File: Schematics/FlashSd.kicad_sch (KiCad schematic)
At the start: 4 parts, among them J8 Micro_SD_Card

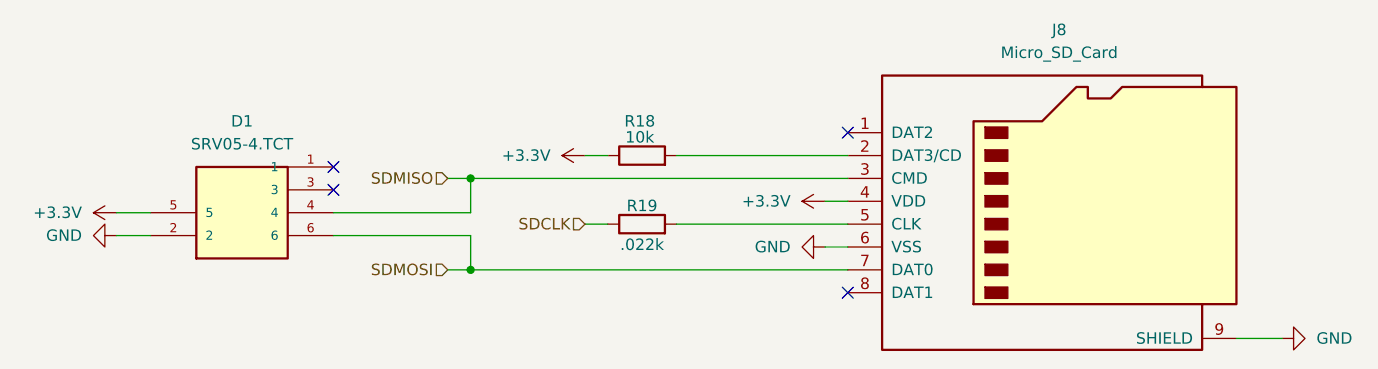
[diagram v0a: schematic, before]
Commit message: added LCSC numbers and footprint values, need to connect schemeatic pins, then can start layout
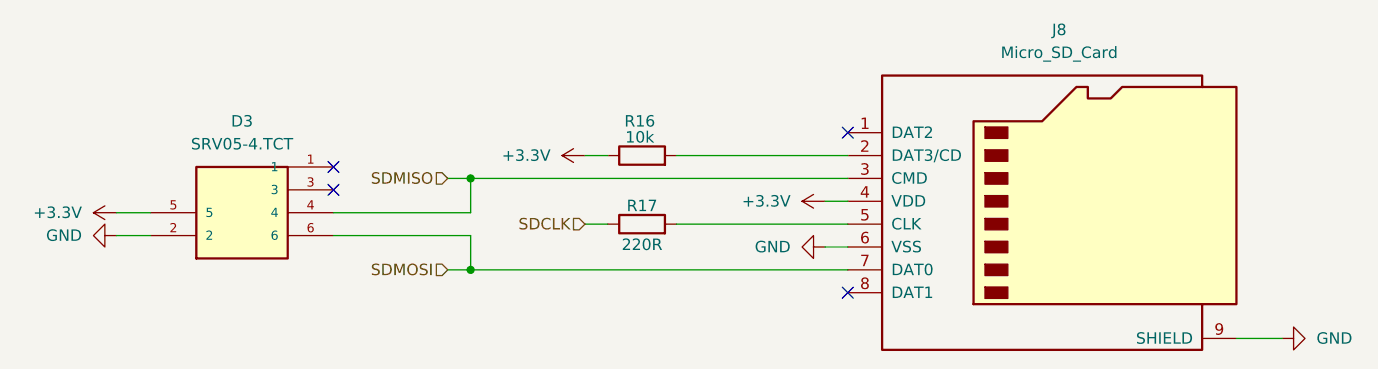
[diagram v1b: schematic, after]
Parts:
- D3: renamed from D1; LCSC Part (none) -> C13612
- J8: footprint (none) -> Connector_Card:microSD_HC_Molex_104031-0811; LCSC Part (none) -> C164170
- R16: renamed from R18; footprint (none) -> Resistor_SMD:R_0805_2012Metric_Pad1.20x1.40mm_HandSolder; LCSC Part (none) -> C84376
- R17: renamed from R19; value .022k -> 220R; footprint (none) -> Resistor_SMD:R_0805_2012Metric_Pad1.20x1.40mm_HandSolder; LCSC Part (none) -> C17557
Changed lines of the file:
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@@
 		(on_board yes)
 		(dnp no)
-		(property "Reference" "#PWR043"
+		(property "Reference" "#PWR061"
 			(at 172.72 96.52 0)
 			(effects
@@
 			(project ""
 				(path "/6cb3dda3-5fe8-4715-b831-354360aa3199/caa4144d-1f54-4913-83e9-888ee3d0dcec"
-					(reference "#PWR043")
+					(reference "#PWR061")
 					(unit 1)
 				)
@@
 		(dnp no)
 		(fields_autoplaced yes)
-		(property "Reference" "#PWR08"
+		(property "Reference" "#PWR063"
 			(at 226.06 111.76 0)
 			(effects
@@
 			(project ""
 				(path "/6cb3dda3-5fe8-4715-b831-354360aa3199/caa4144d-1f54-4913-83e9-888ee3d0dcec"
-					(reference "#PWR08")
+					(reference "#PWR063")
 					(unit 1)
 				)
@@
 		(on_board yes)
 		(dnp no)
-		(property "Reference" "D1"
+		(property "Reference" "D3"
 			(at 104.14 87.63 0)
 			(effects
@@
 				)
 				(justify bottom)
+				(hide yes)
+			)
+		)
+		(property "Sim.Device" ""
+			(at 93.98 95.25 0)
+			(effects
+				(font
+					(size 1.27 1.27)
+				)
+				(hide yes)
+			)
+		)
+		(property "Sim.Type" ""
+			(at 93.98 95.25 0)
+			(effects
+				(font
+					(size 1.27 1.27)
+				)
+				(hide yes)
+			)
+		)
+		(property "LCSC Part" "C13612"
+			(at 93.98 95.25 0)
+			(effects
+				(font
+					(size 1.27 1.27)
+				)
 				(hide yes)
 			)
@@
 			(project "flightcomputer2"
 				(path "/6cb3dda3-5fe8-4715-b831-354360aa3199/caa4144d-1f54-4913-83e9-888ee3d0dcec"
-					(reference "D1")
+					(reference "D3")
 					(unit 1)
 				)
@@
 		(dnp no)
 		(fields_autoplaced yes)
-		(property "Reference" "#PWR045"
+		(property "Reference" "#PWR059"
 			(at 83.82 100.33 0)
 			(effects
@@
 			(project ""
 				(path "/6cb3dda3-5fe8-4715-b831-354360aa3199/caa4144d-1f54-4913-83e9-888ee3d0dcec"
-					(reference "#PWR045")
+					(reference "#PWR059")
 					(unit 1)
 				)
@@
 		(on_board yes)
 		(dnp no)
-		(property "Reference" "R18"
+		(property "Reference" "R16"
 			(at 148.336 87.63 90)
 			(effects
@@
 			)
 		)
-		(property "Footprint" ""
+		(property "Footprint" "Resistor_SMD:R_0805_2012Metric_Pad1.20x1.40mm_HandSolder"
 			(at 148.59 93.218 90)
 			(effects
@@
 		(property "Description" "Resistor"
 			(at 148.59 91.44 0)
+			(effects
+				(font
+					(size 1.27 1.27)
+				)
+				(hide yes)
+			)
+		)
+		(property "Sim.Device" ""
+			(at 148.59 91.44 90)
+			(effects
+				(font
+					(size 1.27 1.27)
+				)
+				(hide yes)
+			)
+		)
+		(property "Sim.Type" ""
+			(at 148.59 91.44 90)
+			(effects
+				(font
+					(size 1.27 1.27)
+				)
+				(hide yes)
+			)
+		)
+		(property "LCSC Part" "C84376"
+			(at 148.59 91.44 90)
 			(effects
 				(font
@@
 			(project ""
 				(path "/6cb3dda3-5fe8-4715-b831-354360aa3199/caa4144d-1f54-4913-83e9-888ee3d0dcec"
-					(reference "R18")
+					(reference "R16")
 					(unit 1)
 				)
@@
 		(on_board yes)
 		(dnp no)
-		(property "Reference" "R19"
+		(property "Reference" "R17"
 			(at 148.59 97.028 90)
 			(effects
@@
 			)
 		)
-		(property "Value" ".022k"
+		(property "Value" "220R"
 			(at 148.59 101.346 90)
 			(effects
@@
 			)
 		)
-		(property "Footprint" ""
+		(property "Footprint" "Resistor_SMD:R_0805_2012Metric_Pad1.20x1.40mm_HandSolder"
 			(at 148.59 100.838 90)
 			(effects
@@
 		(property "Description" "Resistor"
 			(at 148.59 99.06 0)
+			(effects
+				(font
+					(size 1.27 1.27)
+				)
+				(hide yes)
+			)
+		)
+		(property "Sim.Device" ""
+			(at 148.59 99.06 90)
+			(effects
+				(font
+					(size 1.27 1.27)
+				)
+				(hide yes)
+			)
+		)
+		(property "Sim.Type" ""
+			(at 148.59 99.06 90)
+			(effects
+				(font
+					(size 1.27 1.27)
+				)
+				(hide yes)
+			)
+		)
+		(property "LCSC Part" "C17557"
+			(at 148.59 99.06 90)
 			(effects
 				(font
@@
 			(project ""
 				(path "/6cb3dda3-5fe8-4715-b831-354360aa3199/caa4144d-1f54-4913-83e9-888ee3d0dcec"
-					(reference "R19")
+					(reference "R17")
 					(unit 1)
 				)
@@
 		(dnp no)
 		(fields_autoplaced yes)
-		(property "Reference" "#PWR044"
+		(property "Reference" "#PWR058"
 			(at 93.98 97.79 0)
 			(effects
@@
 			(project ""
 				(path "/6cb3dda3-5fe8-4715-b831-354360aa3199/caa4144d-1f54-4913-83e9-888ee3d0dcec"
-					(reference "#PWR044")
+					(reference "#PWR058")
 					(unit 1)
 				)
@@
 		(dnp no)
 		(fields_autoplaced yes)
-		(property "Reference" "#PWR046"
+		(property "Reference" "#PWR062"
 			(at 162.56 101.6 0)
 			(effects
@@
 			(project ""
 				(path "/6cb3dda3-5fe8-4715-b831-354360aa3199/caa4144d-1f54-4913-83e9-888ee3d0dcec"
-					(reference "#PWR046")
+					(reference "#PWR062")
 					(unit 1)
 				)
@@
 			)
 		)
-		(property "Footprint" ""
+		(property "Footprint" "Connector_Card:microSD_HC_Molex_104031-0811"
 			(at 223.52 88.9 0)
 			(effects
@@
 		)
 		(property "Description" "Micro SD Card Socket"
+			(at 194.31 96.52 0)
+			(effects
+				(font
+					(size 1.27 1.27)
+				)
+				(hide yes)
+			)
+		)
+		(property "LCSC Part" "C164170"
+			(at 194.31 96.52 0)
+			(effects
+				(font
+					(size 1.27 1.27)
+				)
+				(hide yes)
+			)
+		)
+		(property "Sim.Device" ""
+			(at 194.31 96.52 0)
+			(effects
+				(font
+					(size 1.27 1.27)
+				)
+				(hide yes)
+			)
+		)
+		(property "Sim.Type" ""
 			(at 194.31 96.52 0)
 			(effects
@@
 		(dnp no)
 		(fields_autoplaced yes)
-		(property "Reference" "#PWR070"
+		(property "Reference" "#PWR060"
 			(at 146.05 91.44 0)
 			(effects
@@
 			(project ""
 				(path "/6cb3dda3-5fe8-4715-b831-354360aa3199/caa4144d-1f54-4913-83e9-888ee3d0dcec"
-					(reference "#PWR070")
+					(reference "#PWR060")
 					(unit 1)
 				)

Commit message: started lora schematic all pcb parts should be included
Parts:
- D3: DESCRIPTION Semtech SRV05-4.TCT, Uni-Directional TVS Diode Array, 300W,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 -> (none); Description_1 ESD Suppressors / TVS Diodes SOT-23 5V 4DIODE Low Capacitan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 -> (none); MF UMW -> (none); MOUSER_PART_NUMBER 947-SRV05-4.TCT -> (none); MOUSER_PRICE-STOCK https://www.mouser.com/Search/Refine.aspx?Keyword=947-SRV05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 -> (none); MP SRV05-4.TCT -> (none); Package None -> (none); Price None -> (none)
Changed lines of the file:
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@@
 			)
 		)
-		(property "MF" "UMW"
+		(property "Check_prices" "https://www.snapeda.com/parts/SRV05-4.TCT/UMW/view-part/?ref=eda"
 			(at 93.98 95.25 0)
 			(effects
@@
 			)
 		)
-		(property "MOUSER_PRICE-STOCK" "https://www.mouser.com/Search/Refine.aspx?Keyword=947-SRV05-4.TCT"
+		(property "HEIGHT" "1.45mm"
 			(at 93.98 95.25 0)
 			(effects
@@
 			)
 		)
-		(property "DESCRIPTION" "Semtech SRV05-4.TCT, Uni-Directional TVS Diode Array, 300W, 6-Pin SOT-23"
+		(property "SnapEDA_Link" "https://www.snapeda.com/parts/SRV05-4.TCT/UMW/view-part/?ref=snap"
 			(at 93.98 95.25 0)
 			(effects
@@
 			)
 		)
-		(property "MOUSER_PART_NUMBER" "947-SRV05-4.TCT"
+		(property "Availability" "In Stock"
 			(at 93.98 95.25 0)
 			(effects
@@
 			)
 		)
-		(property "Price" "None"
+		(property "MANUFACTURER_PART_NUMBER" "SRV05-4.TCT"
 			(at 93.98 95.25 0)
 			(effects
@@
 				)
 				(justify bottom)
-				(hide yes)
-			)
-		)
-		(property "Package" "None"
-			(at 93.98 95.25 0)
-			(effects
-				(font
-					(size 1.27 1.27)
-				)
-				(justify bottom)
-				(hide yes)
-			)
-		)
-		(property "Check_prices" "https://www.snapeda.com/parts/SRV05-4.TCT/UMW/view-part/?ref=eda"
-			(at 93.98 95.25 0)
-			(effects
-				(font
-					(size 1.27 1.27)
-				)
-				(justify bottom)
-				(hide yes)
-			)
-		)
-		(property "HEIGHT" "1.45mm"
-			(at 93.98 95.25 0)
-			(effects
-				(font
-					(size 1.27 1.27)
-				)
-				(justify bottom)
-				(hide yes)
-			)
-		)
-		(property "SnapEDA_Link" "https://www.snapeda.com/parts/SRV05-4.TCT/UMW/view-part/?ref=snap"
-			(at 93.98 95.25 0)
-			(effects
-				(font
-					(size 1.27 1.27)
-				)
-				(justify bottom)
-				(hide yes)
-			)
-		)
-		(property "MP" "SRV05-4.TCT"
-			(at 93.98 95.25 0)
-			(effects
-				(font
-					(size 1.27 1.27)
-				)
-				(justify bottom)
-				(hide yes)
-			)
-		)
-		(property "Description_1" "ESD Suppressors / TVS Diodes SOT-23 5V 4DIODE Low Capacitance"
-			(at 93.98 95.25 0)
-			(effects
-				(font
-					(size 1.27 1.27)
-				)
-				(justify bottom)
-				(hide yes)
-			)
-		)
-		(property "Availability" "In Stock"
-			(at 93.98 95.25 0)
-			(effects
-				(font
-					(size 1.27 1.27)
-				)
-				(justify bottom)
-				(hide yes)
-			)
-		)
-		(property "MANUFACTURER_PART_NUMBER" "SRV05-4.TCT"
-			(at 93.98 95.25 0)
-			(effects
-				(font
-					(size 1.27 1.27)
-				)
-				(justify bottom)
-				(hide yes)
-			)
-		)
-		(property "Sim.Device" ""
-			(at 93.98 95.25 0)
-			(effects
-				(font
-					(size 1.27 1.27)
-				)
-				(hide yes)
-			)
-		)
-		(property "Sim.Type" ""
-			(at 93.98 95.25 0)
-			(effects
-				(font
-					(size 1.27 1.27)
-				)
 				(hide yes)
 			)
@@
 			)
 		)
-		(property "Sim.Device" ""
-			(at 148.59 91.44 90)
-			(effects
-				(font
-					(size 1.27 1.27)
-				)
-				(hide yes)
-			)
-		)
-		(property "Sim.Type" ""
-			(at 148.59 91.44 90)
-			(effects
-				(font
-					(size 1.27 1.27)
-				)
-				(hide yes)
-			)
-		)
 		(property "LCSC Part" "C84376"
 			(at 148.59 91.44 90)
@@
 		(property "Description" "Resistor"
 			(at 148.59 99.06 0)
-			(effects
-				(font
-					(size 1.27 1.27)
-				)
-				(hide yes)
-			)
-		)
-		(property "Sim.Device" ""
-			(at 148.59 99.06 90)
-			(effects
-				(font
-					(size 1.27 1.27)
-				)
-				(hide yes)
-			)
-		)
-		(property "Sim.Type" ""
-			(at 148.59 99.06 90)
 			(effects
 				(font
@@
 			(at 194.31 96.52 0)
 			(effects
-				(font
-					(size 1.27 1.27)
-				)
-				(hide yes)
-			)
-		)
-		(property "Sim.Device" ""
-			(at 194.31 96.52 0)
-			(effects
-				(font
-					(size 1.27 1.27)
-				)
-				(hide yes)
-			)
-		)
-		(property "Sim.Type" ""
-			(at 194.31 96.52 0)
-			(effects

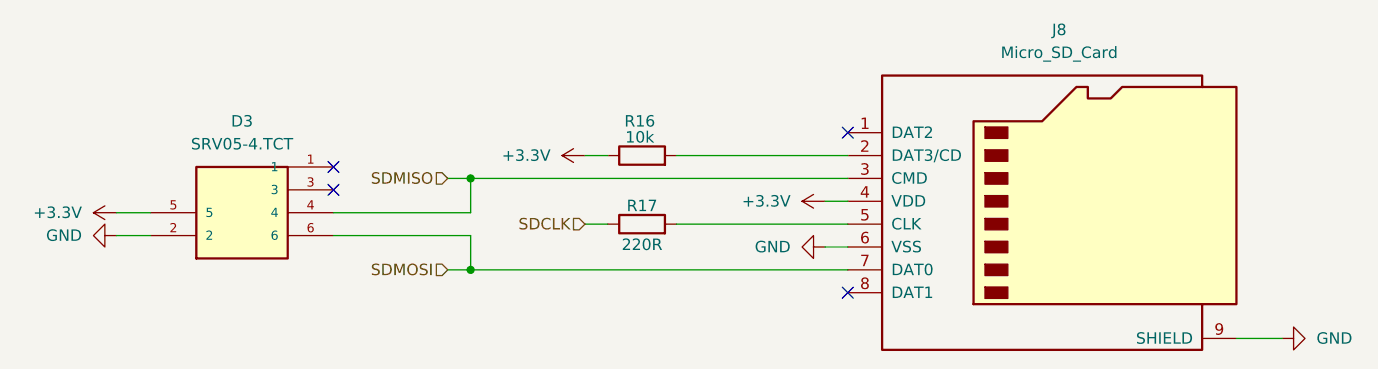
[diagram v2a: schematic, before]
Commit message: added lora correct and organizing sheet pins
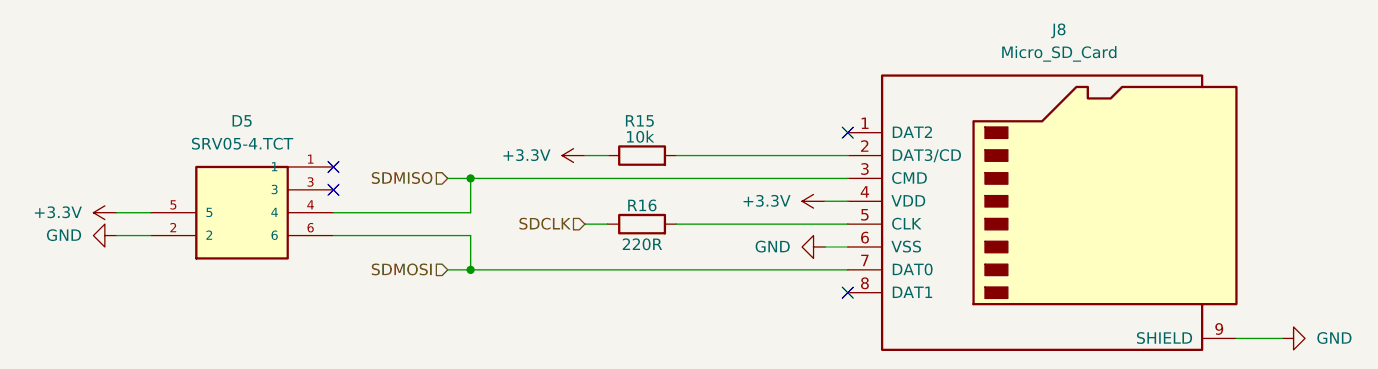
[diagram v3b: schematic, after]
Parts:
- J8: footprint Connector_Card:microSD_HC_Molex_104031-0811 -> Connector_Card:microSD_HC_Molex_47219-2001
- renumbered D3 to D5, R16 to R15, R17 to R16
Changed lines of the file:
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@@
 		(on_board yes)
 		(dnp no)
-		(property "Reference" "#PWR061"
+		(property "Reference" "#PWR064"
 			(at 172.72 96.52 0)
 			(effects
@@
 			(project ""
 				(path "/6cb3dda3-5fe8-4715-b831-354360aa3199/caa4144d-1f54-4913-83e9-888ee3d0dcec"
-					(reference "#PWR061")
+					(reference "#PWR064")
 					(unit 1)
 				)
@@
 		(dnp no)
 		(fields_autoplaced yes)
-		(property "Reference" "#PWR063"
+		(property "Reference" "#PWR066"
 			(at 226.06 111.76 0)
 			(effects
@@
 			(project ""
 				(path "/6cb3dda3-5fe8-4715-b831-354360aa3199/caa4144d-1f54-4913-83e9-888ee3d0dcec"
-					(reference "#PWR063")
+					(reference "#PWR066")
 					(unit 1)
 				)
@@
 		(on_board yes)
 		(dnp no)
-		(property "Reference" "D3"
+		(property "Reference" "D5"
 			(at 104.14 87.63 0)
 			(effects
@@
 			(project "flightcomputer2"
 				(path "/6cb3dda3-5fe8-4715-b831-354360aa3199/caa4144d-1f54-4913-83e9-888ee3d0dcec"
-					(reference "D3")
+					(reference "D5")
 					(unit 1)
 				)
@@
 		(dnp no)
 		(fields_autoplaced yes)
-		(property "Reference" "#PWR059"
+		(property "Reference" "#PWR062"
 			(at 83.82 100.33 0)
 			(effects
@@
 			(project ""
 				(path "/6cb3dda3-5fe8-4715-b831-354360aa3199/caa4144d-1f54-4913-83e9-888ee3d0dcec"
-					(reference "#PWR059")
+					(reference "#PWR062")
 					(unit 1)
 				)
@@
 		(on_board yes)
 		(dnp no)
-		(property "Reference" "R16"
+		(property "Reference" "R15"
 			(at 148.336 87.63 90)
 			(effects
@@
 			(project ""
 				(path "/6cb3dda3-5fe8-4715-b831-354360aa3199/caa4144d-1f54-4913-83e9-888ee3d0dcec"
-					(reference "R16")
+					(reference "R15")
 					(unit 1)
 				)
@@
 		(on_board yes)
 		(dnp no)
-		(property "Reference" "R17"
+		(property "Reference" "R16"
 			(at 148.59 97.028 90)
 			(effects
@@
 			(project ""
 				(path "/6cb3dda3-5fe8-4715-b831-354360aa3199/caa4144d-1f54-4913-83e9-888ee3d0dcec"
-					(reference "R17")
+					(reference "R16")
 					(unit 1)
 				)
@@
 		(dnp no)
 		(fields_autoplaced yes)
-		(property "Reference" "#PWR058"
+		(property "Reference" "#PWR061"
 			(at 93.98 97.79 0)
 			(effects
@@
 			(project ""
 				(path "/6cb3dda3-5fe8-4715-b831-354360aa3199/caa4144d-1f54-4913-83e9-888ee3d0dcec"
-					(reference "#PWR058")
+					(reference "#PWR061")
 					(unit 1)
 				)
@@
 		(dnp no)
 		(fields_autoplaced yes)
-		(property "Reference" "#PWR062"
+		(property "Reference" "#PWR065"
 			(at 162.56 101.6 0)
 			(effects
@@
 			(project ""
 				(path "/6cb3dda3-5fe8-4715-b831-354360aa3199/caa4144d-1f54-4913-83e9-888ee3d0dcec"
-					(reference "#PWR062")
+					(reference "#PWR065")
 					(unit 1)
 				)
@@
 			)
 		)
-		(property "Footprint" "Connector_Card:microSD_HC_Molex_104031-0811"
+		(property "Footprint" "Connector_Card:microSD_HC_Molex_47219-2001"
 			(at 223.52 88.9 0)
 			(effects
@@
 		(dnp no)
 		(fields_autoplaced yes)
-		(property "Reference" "#PWR060"
+		(property "Reference" "#PWR063"
 			(at 146.05 91.44 0)
 			(effects
@@
 			(project ""
 				(path "/6cb3dda3-5fe8-4715-b831-354360aa3199/caa4144d-1f54-4913-83e9-888ee3d0dcec"
-					(reference "#PWR060")
-					(unit 1)
-				)
+					(reference "#PWR063")
+					(unit 1)
+				)

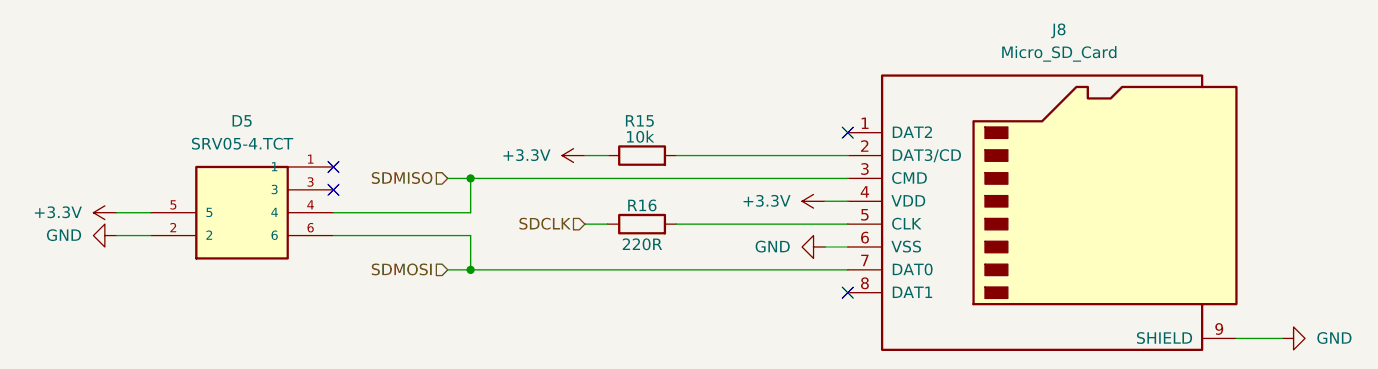
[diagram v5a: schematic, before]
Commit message: fixing DRC Warnings updated USBC footprint/schematic, did impedance matching for the trace from rfm95 to antenna connector fixed resistor on flash memeory
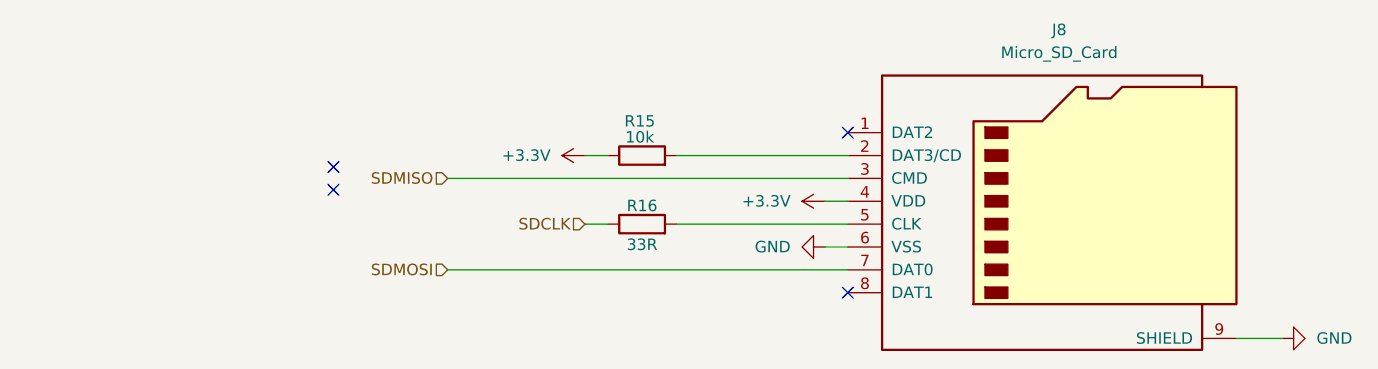
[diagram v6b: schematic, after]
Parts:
- removed D5: SRV05-4.TCT, myFootprints:SOT95P280X145-6N, symbol SRV05-4.TCT:SRV05-4.TCT
- R16: value 220R -> 33R

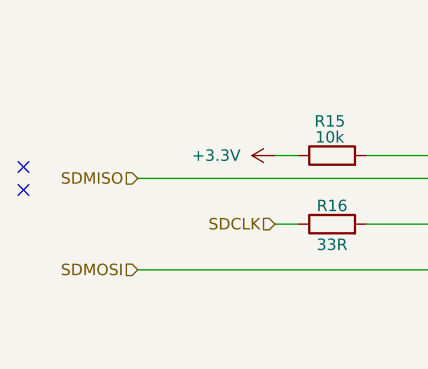
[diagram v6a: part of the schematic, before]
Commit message: added final lcsc parts
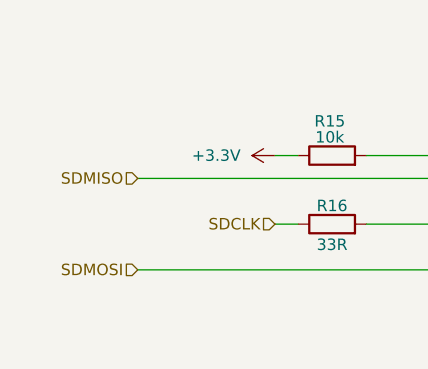
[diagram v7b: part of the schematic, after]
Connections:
- no-connect marks 4 -> 2
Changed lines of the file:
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@@
-	)
-	(no_connect
-		(at 114.3 95.25)
-	)
-	(no_connect
-		(at 114.3 92.71)
 	)
 	(no_connect
